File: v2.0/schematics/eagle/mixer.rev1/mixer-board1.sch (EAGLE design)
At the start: 61 parts, among them IC1 TL084P, IC2 TL084P, J1 M1, J2 M2, J3 SEND1, J4 SEND2, J5 ST1-L, J6 ST1-R, J7 ST2-L, J8 ST2-R

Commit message: Completed initial mixer schematic draft
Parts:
- added C21, C22, C23, C24, C31, C32, C33, C34, C35, C36, C41, C42, C43, C44: 100uF, _common:CE-USE2-5
- added C25, C26, C27, C28, C29, C30, C37, C38, C39, C40: 22pF, _common:CC-US025-024X044
- added IC3, IC4: TL082P, _common:TL082P
- added JP1: PWR, pinhead:PINHD-2X5
- added JP2, JP4: (no value), pinhead:PINHD-2X8
- added JP3, JP5: (no value), pinhead:PINHD-2X5
- added R32, R33, R34, R35, R36, R37, R38, R43, R44: 5.1K, _common:R
- added R39, R40, R41, R42: 2.7K, _common:R
- added R45, R46: 10K, _common:R
- C1, C2: value 100uF -> 10uF; device _common:CE-USE2-5 -> _common.v1:CE-USE2-5
- C10, C11, C12, C4, C9: value 100uF -> 0.1uF; device _common:CE-USE2-5 -> _common.v1:CC-US025-024X044
- C15, C16, C17: value 20pF -> 100uF; device _common:CC-US025-024X044 -> _common:CE-USE2-5
- C3, C5, C6, C7, C8: value 20pF -> 0.1uF; device _common:CC-US025-024X044 -> _common.v1:CC-US025-024X044
- IC1: value TL084P -> TL082P; device _common:TL084P -> _common:TL082P
- J1: value M1 -> M2
- J2: value M2 -> ST1-L
- J3: value SEND1 -> ST1-R
- J4: value SEND2 -> ST2-L
- J5: value ST1-L -> ST2-R
- J6: value ST1-R -> M1
- J7: value ST2-L -> SEND1
- J8: value ST2-R -> SEND2
- R10, R11, R6, R9: value 2.7K -> 100K
- R12, R5, R7, R8: value 5.1K -> 100K
- R13, R14: value 5.1K -> 510
- R15, R16: value 10K -> 510
- R17, R18: value 100K -> 510
- R19, R20, R21, R22: value 100K -> 1K
- R25: value 1K -> 5.1K
- R28, R29, R30: value 510 -> 5.1K
- R3: value 1K -> 100K
- R4: value 510 -> 100K
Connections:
- removed net FX-MX-1: R31.2
- removed net N$16: C12.-, R18.1
- removed net N$17: IC1C.+IN, R18.2, R21.2
- removed net N$19: C16.2, IC1C.-IN, R24.1, R29.2
- removed net N$20: C16.1, C19.+, IC1C.OUT, R24.2
- removed net N$21: C19.-, R26.1, R31.1
- removed net SEND1-OUT: R26.2
- new net +12V: C1.+, C11.1, C3.1, C5.1, C7.1, C9.1, IC1P.V+, IC2P.V+, IC3P.V+, IC4P.V+, JP1.10, JP1.9, JP4.5, JP5.5
- new net -12V: C10.2, C12.2, C2.-, C4.2, C6.2, C8.2, IC1P.V-, IC2P.V-, IC3P.V-, IC4P.V-, JP1.1, JP1.2, JP4.1, JP5.1
- new net FX1-1-SEND1: C41.-, JP3.1, JP4.11
- new net FX1-2-MIX-L: JP3.3, R35.1
- new net FX1-3-RTN1-L: JP3.5, JP4.2
- new net FX1-5-MIX-R: JP3.7, R36.1
- new net FX1-6-RTN1-R: JP3.9, JP4.4
- new net FX2-1-SEND2: C42.-, JP3.2, JP4.13
- new net FX2-2-MIX-L: JP3.4, R37.1
- new net FX2-3-RTN2-L: JP3.6, JP4.6
- new net FX2-5-MIX-R: JP3.8, R38.1
- new net FX2-6-RTN2-R: JP3.10, JP4.8
- new net M2-LVL-2: JP4.9, R2.1
- new net M2-LVL-3: C14.-, JP4.7
- new net N$22: C26.1, C32.+, IC1B.OUT, R20.2
- new net N$23: C26.2, IC1B.-IN, R14.2, R20.1
- new net N$24: C20.-, IC1B.+IN, R8.2
- new net N$25: C20.+, R2.2
- new net N$26: C14.+, J1.P$4
- new net N$28: C34.-, R30.1
- new net N$29: C33.-, R29.1
- new net N$30: C27.1, C33.+, IC2A.OUT, R21.2
- new net N$31: C27.2, IC2A.-IN, R15.2, R21.1
- new net N$32: C21.-, IC2A.+IN, R9.2
- new net N$33: C21.+, R3.2
- new net N$34: C15.+, J2.P$4
- new net N$35: C28.1, C34.+, IC2B.OUT, R22.2
- new net N$36: C28.2, IC2B.-IN, R16.2, R22.1
- new net N$37: C22.-, IC2B.+IN, R10.2
- new net N$38: C22.+, R4.2
- new net N$39: C16.+, J3.P$4
- new net N$41: C35.-, R31.1
- new net N$42: C29.1, C35.+, IC2C.OUT, R23.2
- new net N$43: C29.2, IC2C.-IN, R17.2, R23.1
- new net N$44: C23.-, IC2C.+IN, R11.2
- new net N$45: C23.+, R5.2
- new net N$46: C17.+, J4.P$4
- new net N$48: C36.-, R32.1
- new net N$49: C30.1, C36.+, IC2D.OUT, R24.2
- new net N$50: C30.2, IC2D.-IN, R18.2, R24.1
- new net N$51: C24.-, IC2D.+IN, R12.2
- new net N$52: C24.+, R6.2
- new net N$53: C18.+, J5.P$4
- new net N$58: C42.+, J8.P$4
- new net ST1-LVL-2: R3.1
- new net ST1-LVL-3: C15.-, JP2.7
- new net ST1-LVL-5: JP2.13, R4.1
- new net ST1-LVL-6: C16.-, JP2.11
- new net ST1-LVL2: JP2.9
- new net ST2-LVL-2: JP2.10, R5.1
- new net ST2-LVL-3: C17.-, JP2.8
- new net ST2-LVL-5: JP2.14, R6.1
- new net ST2-LVL-6: C18.-, JP2.12
- new net ST3-L: JP5.7, R33.1
- new net ST3-R: JP5.9, R34.1
- net 0V: now also C1.-, C10.1, C11.2, C12.1, C2.+, C3.2, C4.1, C5.2, C6.1, C7.2, C8.1, C9.2, IC3A.+IN, IC3B.+IN, IC4A.+IN, IC4B.+IN, J2.P$1, J2.P$2, J2.P$3, J4.P$1, J4.P$2, J4.P$3, J5.P$1, J5.P$2, J5.P$3, J6.P$1, J6.P$2, J6.P$3, J7.P$1, J7.P$2, J7.P$3, J8.P$1, J8.P$2, J8.P$3, JP1.3, JP1.4, JP1.5, JP1.6, JP1.7, JP1.8, JP2.1, JP2.15, JP2.16, JP2.2, JP4.3, JP5.3, R10.1, R11.1, R12.1, R13.1, R14.1, R17.1, R18.1, R45.1, R46.1, R7.1, R8.1, R9.1; no longer IC2A.+IN, IC2B.+IN, IC2C.+IN, IC2D.+IN, R2.1, R21.1, R29.1, R4.1
- net M1-LVL-2: now also JP2.5
- net M1-LVL-3: now also C13.-, JP2.3; no longer C1.-
- net N$1: now also C13.+, J6.P$4; no longer C1.+, J1.P$4
- net N$10: now also C32.-, R27.1, R28.1; no longer R13.1, R14.1
- net N$11: now also C38.1, IC4A.OUT, R40.2, R42.1; no longer C7.1, IC2C.OUT, R11.1, R9.2
- net N$12: now also C40.2, IC4B.-IN, R42.2, R44.1; no longer C8.2, IC2D.-IN, R11.2, R8.1
- net N$13: now also C39.1, C43.-, IC3B.OUT, R43.2; no longer C6.1, C9.-, IC2B.OUT, R7.2
- net N$14: now also C41.+, J7.P$4; no longer C12.+, J3.P$4
- net N$15: now also C38.2, IC4A.-IN, R26.2, R28.2, R30.2, R32.2, R34.2, R36.2, R38.2, R40.1; no longer C7.2, IC2C.-IN, R12.2, R14.2, R9.1
- net N$18: now also C40.1, C44.-, IC4B.OUT, R44.2; no longer C10.-, C8.1, IC2D.OUT, R8.2
- net N$2: now also C25.2, R13.2, R19.1; no longer C3.2, R3.1, R4.2
- net N$3: now also C19.-, R7.2; no longer C2.-, R2.2
- net N$4: now also C19.+; no longer C2.+
- net N$5: now also C25.1, C31.+, R19.2; no longer C3.1, C4.+, R3.2
- net N$6: now also C31.-, R25.1, R26.1; no longer C4.-, R12.1, R5.1
- net N$7: now also C37.2, IC3A.-IN, R25.2, R27.2, R29.2, R31.2, R33.2, R35.2, R37.2, R39.1; no longer C5.2, IC2A.-IN, R13.2, R5.2, R6.1
- net N$8: now also C37.1, IC3A.OUT, R39.2, R41.1; no longer C5.1, IC2A.OUT, R10.1, R6.2
- net N$9: now also C39.2, IC3B.-IN, R41.2, R43.1; no longer C6.2, IC2B.-IN, R10.2, R7.1
- net OUT-LVL-3: now also C43.+, JP5.2, R45.2; no longer C9.+, R15.2
- net OUT-LVL-6: now also C44.+, JP5.4, R46.2; no longer C10.+, R16.2
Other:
- moved on the sheet: C1, C10, C11, C12, C13, C14, C15, C16, C17, C18, C19, C2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

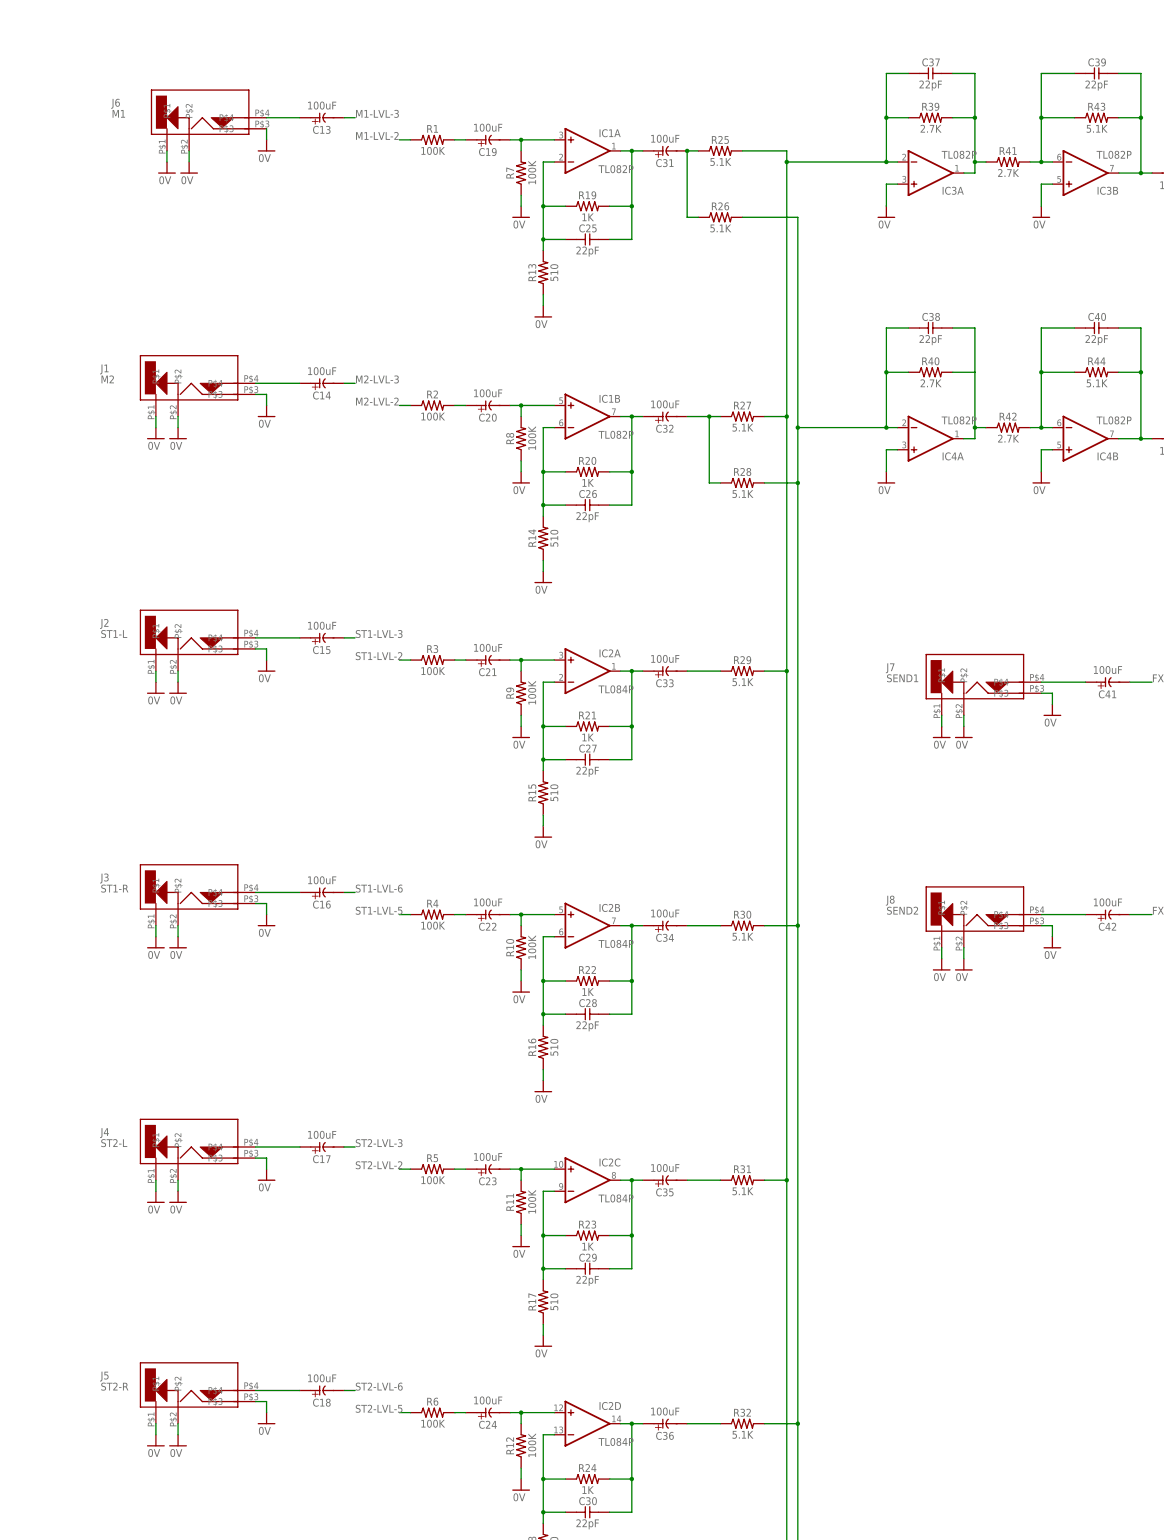
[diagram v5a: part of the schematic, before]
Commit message: Fixed jack grounds; normalled R to L; increased master gain
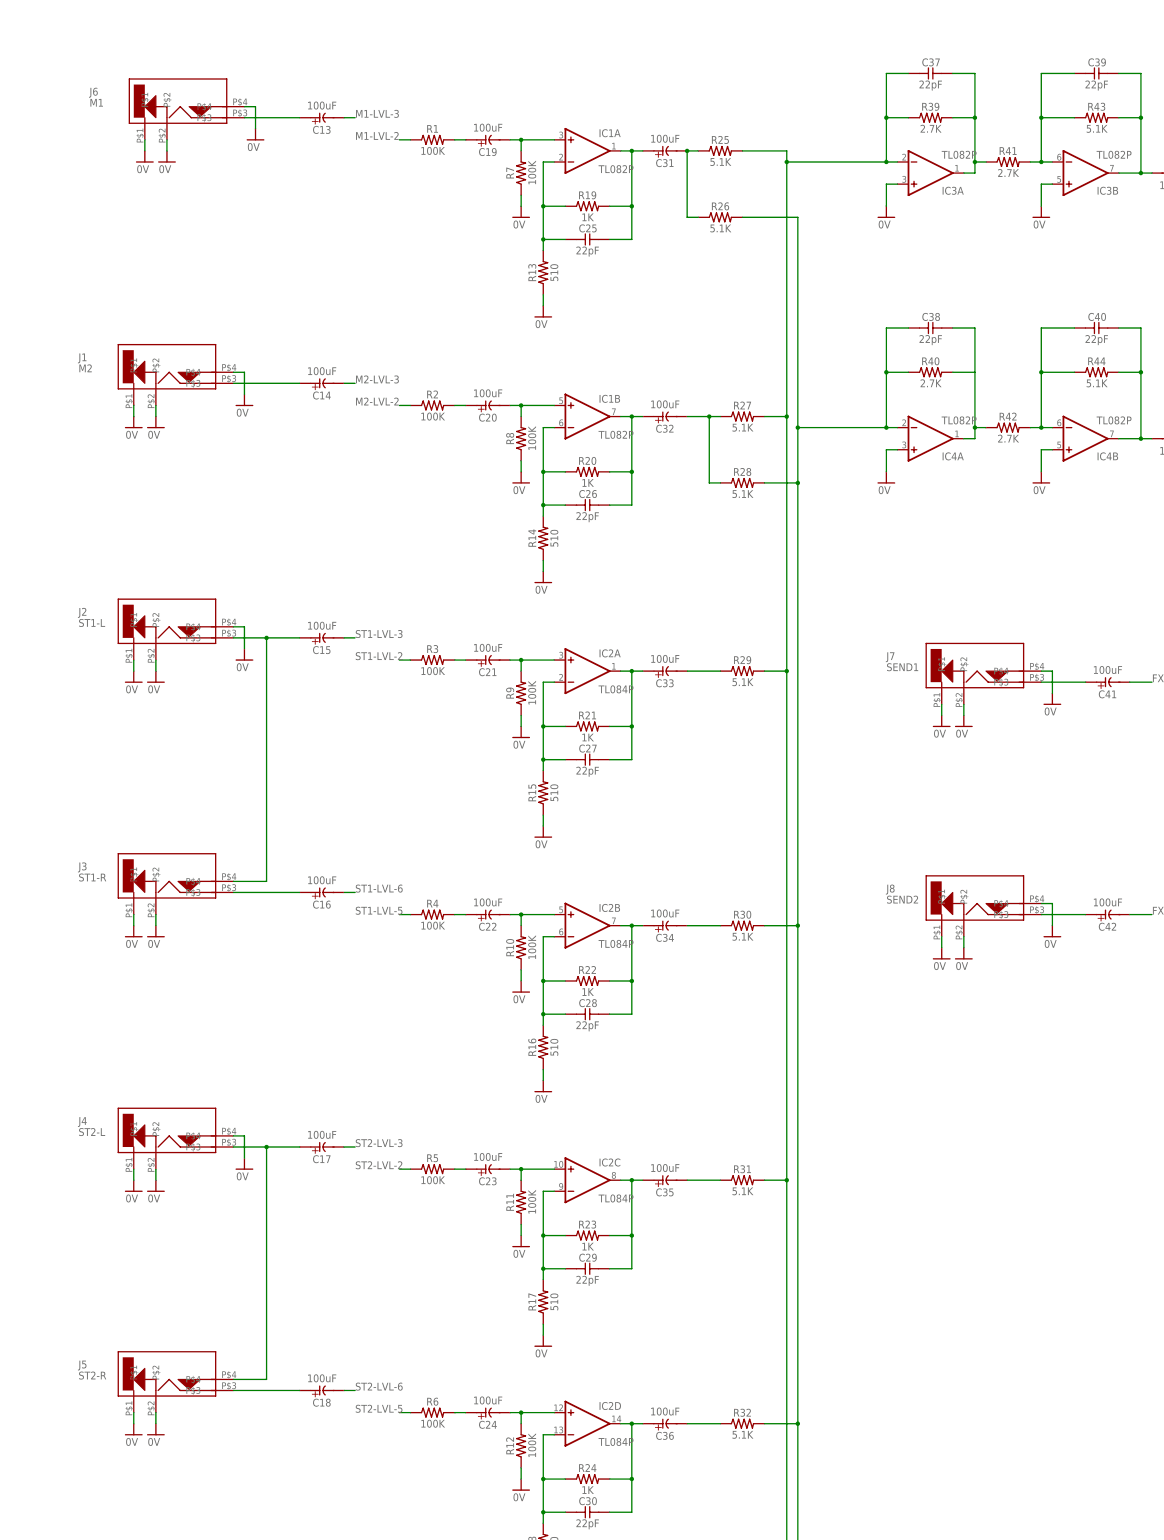
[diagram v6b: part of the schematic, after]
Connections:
- removed net N$26: C14.+, J1.P$4
- removed net N$34: C15.+, J2.P$4
- removed net N$39: C16.+, J3.P$4
- removed net N$46: C17.+, J4.P$4
- removed net N$53: C18.+, J5.P$4
- removed net N$58: C42.+, J8.P$4
- new net N$16: C14.+, J1.P$3
- new net N$17: C15.+, J2.P$3, J3.P$4
- new net N$19: C16.+, J3.P$3
- new net N$20: C17.+, J4.P$3, J5.P$4
- new net N$21: C18.+, J5.P$3
- new net N$27: C41.+, J7.P$3
- net 0V: now also J1.P$4, J2.P$4, J4.P$4, J6.P$4, J7.P$4, J8.P$4; no longer J1.P$3, J2.P$3, J3.P$3, J4.P$3, J5.P$3, J6.P$3, J7.P$3, J8.P$3
- net N$1: now also J6.P$3; no longer J6.P$4
- net N$14: now also C42.+, J8.P$3; no longer C41.+, J7.P$4
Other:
- moved on the sheet: J1, J2, J3, J4, J5, J6, J7, J8

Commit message: Updated VAR-ST; Added FX Crossfades; Ran error checks
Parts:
- removed R45, R46: 10K, _common:R
- JP1: value PWR -> BOARD2-A; device pinhead:PINHD-2X5 -> pinhead:PINHD-2X8
- JP2: value (none) -> BOARD2-B; device pinhead:PINHD-2X8 -> pinhead:PINHD-2X5
- JP3: value (none) -> BOARD3; device pinhead:PINHD-2X5 -> pinhead:PINHD-2X8
- JP4: value (none) -> BOARD4; device pinhead:PINHD-2X8 -> pinhead:PINHD-2X5
- JP5: value (none) -> PWR
- R37, R38: value 5.1K -> 2.7K
- R41, R42: value 2.7K -> 5.1K
- R43, R44: value 5.1K -> 10K
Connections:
- removed net FX1-1-SEND1: C41.-, JP3.1, JP4.11
- removed net FX1-2-MIX-L: JP3.3, R35.1
- removed net FX1-3-RTN1-L: JP3.5, JP4.2
- removed net FX1-5-MIX-R: JP3.7, R36.1
- removed net FX1-6-RTN1-R: JP3.9, JP4.4
- removed net FX2-1-SEND2: C42.-, JP3.2, JP4.13
- removed net FX2-2-MIX-L: JP3.4, R37.1
- removed net FX2-3-RTN2-L: JP3.6, JP4.6
- removed net FX2-5-MIX-R: JP3.8, R38.1
- removed net FX2-6-RTN2-R: JP3.10, JP4.8
- removed net ST1-LVL2: JP2.9
- new net FX-MIX-L: JP2.7, R35.1
- new net FX-MIX-R: JP2.9, R36.1
- new net FX1-RTN-L: JP2.2, JP3.2
- new net FX1-RTN-R: JP2.4, JP3.4
- new net FX1-SEND: C41.-, JP2.3, JP3.11
- new net FX2-RTN-L: JP2.6, JP3.6
- new net FX2-RTN-R: JP2.8, JP3.8
- new net FX2-SEND: C42.-, JP2.5, JP3.13
- net +12V: now also JP1.5, JP3.5, JP5.10, JP5.9; no longer JP1.10, JP1.9, JP5.5
- net -12V: now also JP3.1, JP5.2; no longer JP1.2
- net 0V: now also JP1.14, JP2.10, JP3.14, JP3.3, JP4.8, JP5.4, JP5.5, JP5.6, JP5.7, JP5.8, R43.1, R44.1; no longer JP1.4, JP1.5, JP1.6, JP1.7, JP1.8, JP2.15, JP2.16, JP2.2, R45.1, R46.1
- net M1-LVL-2: now also JP1.10; no longer JP2.5
- net M1-LVL-3: now also JP1.7; no longer JP2.3
- net M2-LVL-2: now also JP3.9; no longer JP4.9
- net M2-LVL-3: now also JP3.7; no longer JP4.7
- net N$11: now also R38.2, R40.1; no longer R40.2, R42.1
- net N$12: now also R40.2, R42.1; no longer R42.2, R44.1
- net N$13: now also R41.2; no longer R43.2
- net N$15: now also R38.1; no longer R38.2, R40.1
- net N$18: now also R42.2; no longer R44.2
- net N$7: now also R37.1; no longer R37.2, R39.1
- net N$8: now also R37.2, R39.1; no longer R39.2, R41.1
- net N$9: now also R39.2, R41.1; no longer R41.2, R43.1
- net OUT-LVL-3: now also JP4.2, R43.2; no longer JP5.2, R45.2
- net OUT-LVL-6: now also JP4.4, R44.2; no longer JP5.4, R46.2
- net ST1-LVL-2: now also JP1.11
- net ST1-LVL-3: now also JP1.9; no longer JP2.7
- net ST1-LVL-5: now also JP1.15; no longer JP2.13
- net ST1-LVL-6: now also JP1.13; no longer JP2.11
- net ST2-LVL-2: now also JP1.4; no longer JP2.10
- net ST2-LVL-3: now also JP1.2; no longer JP2.8
- net ST2-LVL-5: now also JP1.8; no longer JP2.14
- net ST2-LVL-6: now also JP1.6; no longer JP2.12
- net ST3-L: now also JP4.7; no longer JP5.7
- net ST3-R: now also JP4.9; no longer JP5.9
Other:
- moved on the sheet: C1, C10, C11, C12, C2, C3, C4, C5, C6, C7, C8, C9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

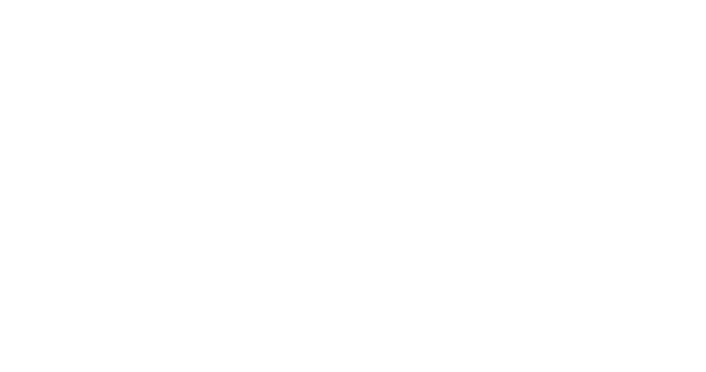
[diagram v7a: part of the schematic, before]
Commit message: Added schem titles
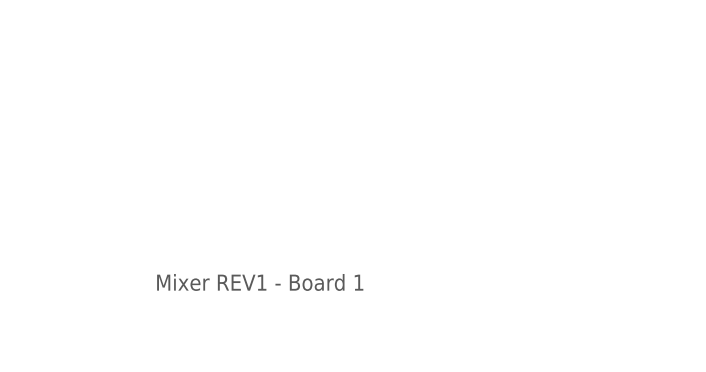
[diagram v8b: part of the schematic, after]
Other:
- note added: "Mixer REV1 - Board 1"
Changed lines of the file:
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@@
 <plain>
 <text x="30.48" y="88.9" size="1.778" layer="97">1/4" TRS - NYS216-U (Neutrik on Mouser) (we have several of the NYS2612-U mono jacks already)</text>
+<text x="-58.42" y="-297.18" size="1.778" layer="97">Mixer REV1 - Board 1</text>
 </plain>
 <instances>
